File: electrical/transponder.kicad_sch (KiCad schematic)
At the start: 3 parts

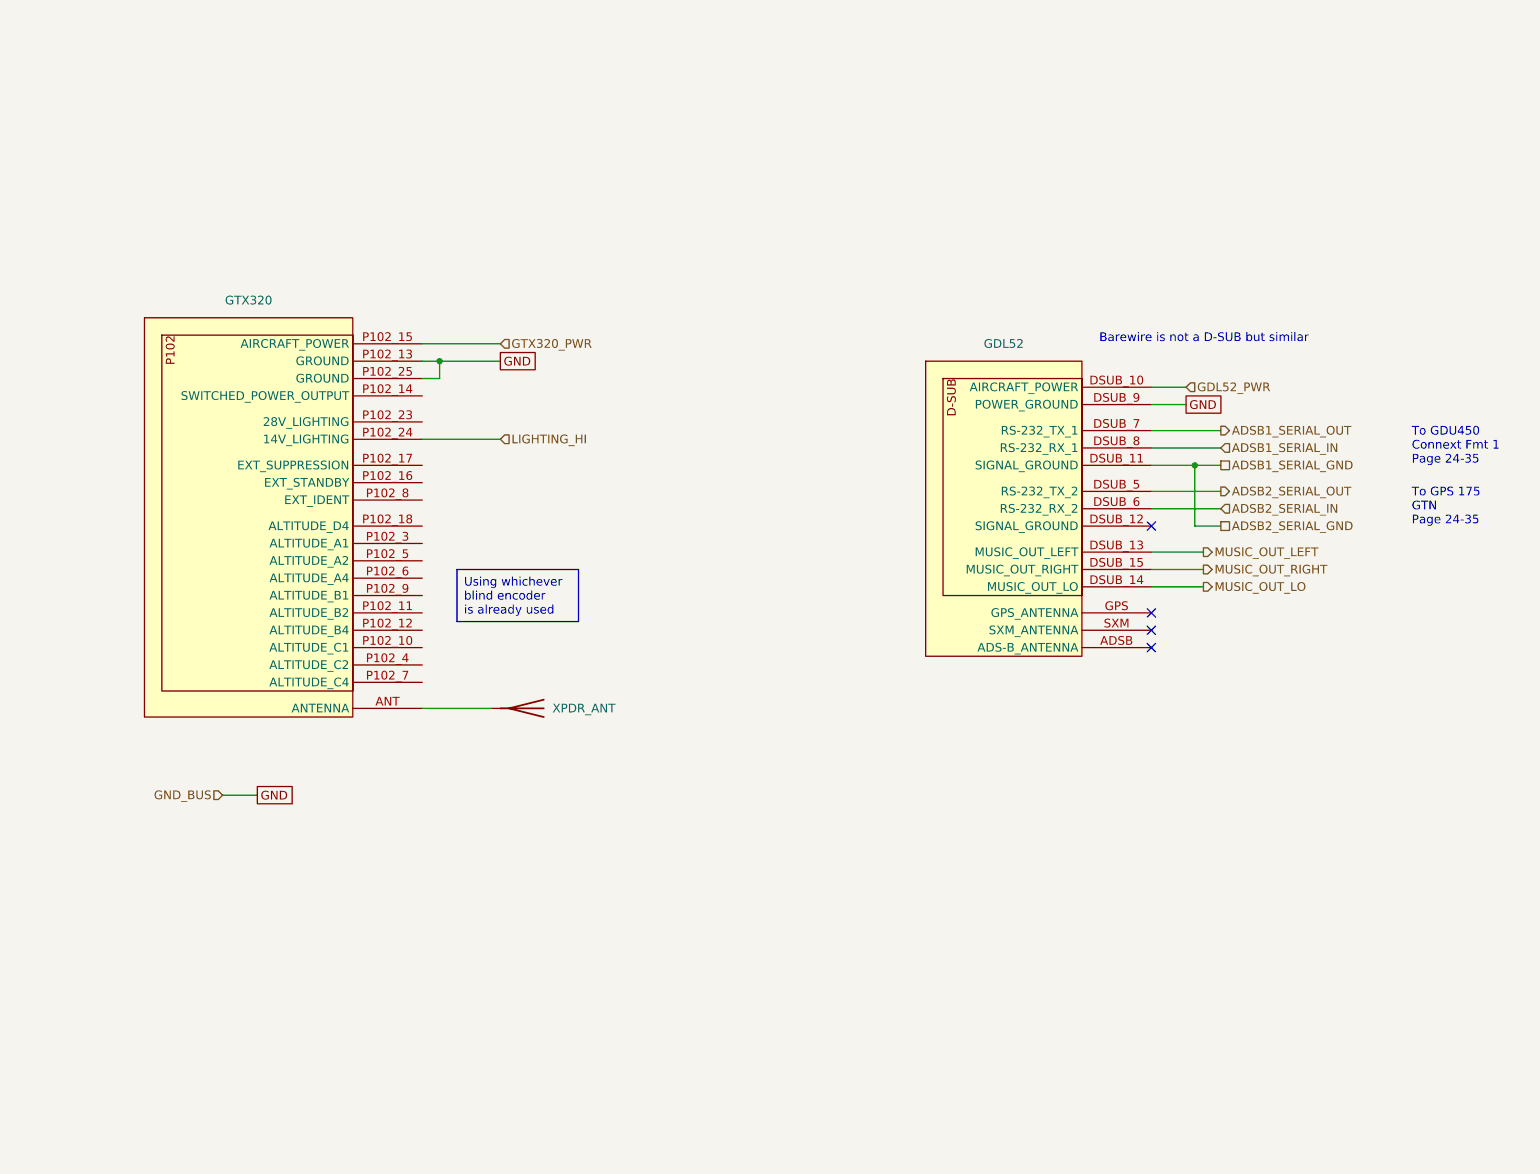
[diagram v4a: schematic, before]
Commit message: Added Altitude Encoder for 320, also added RS232 air data to Transponder in case upgrade to a GTX 327
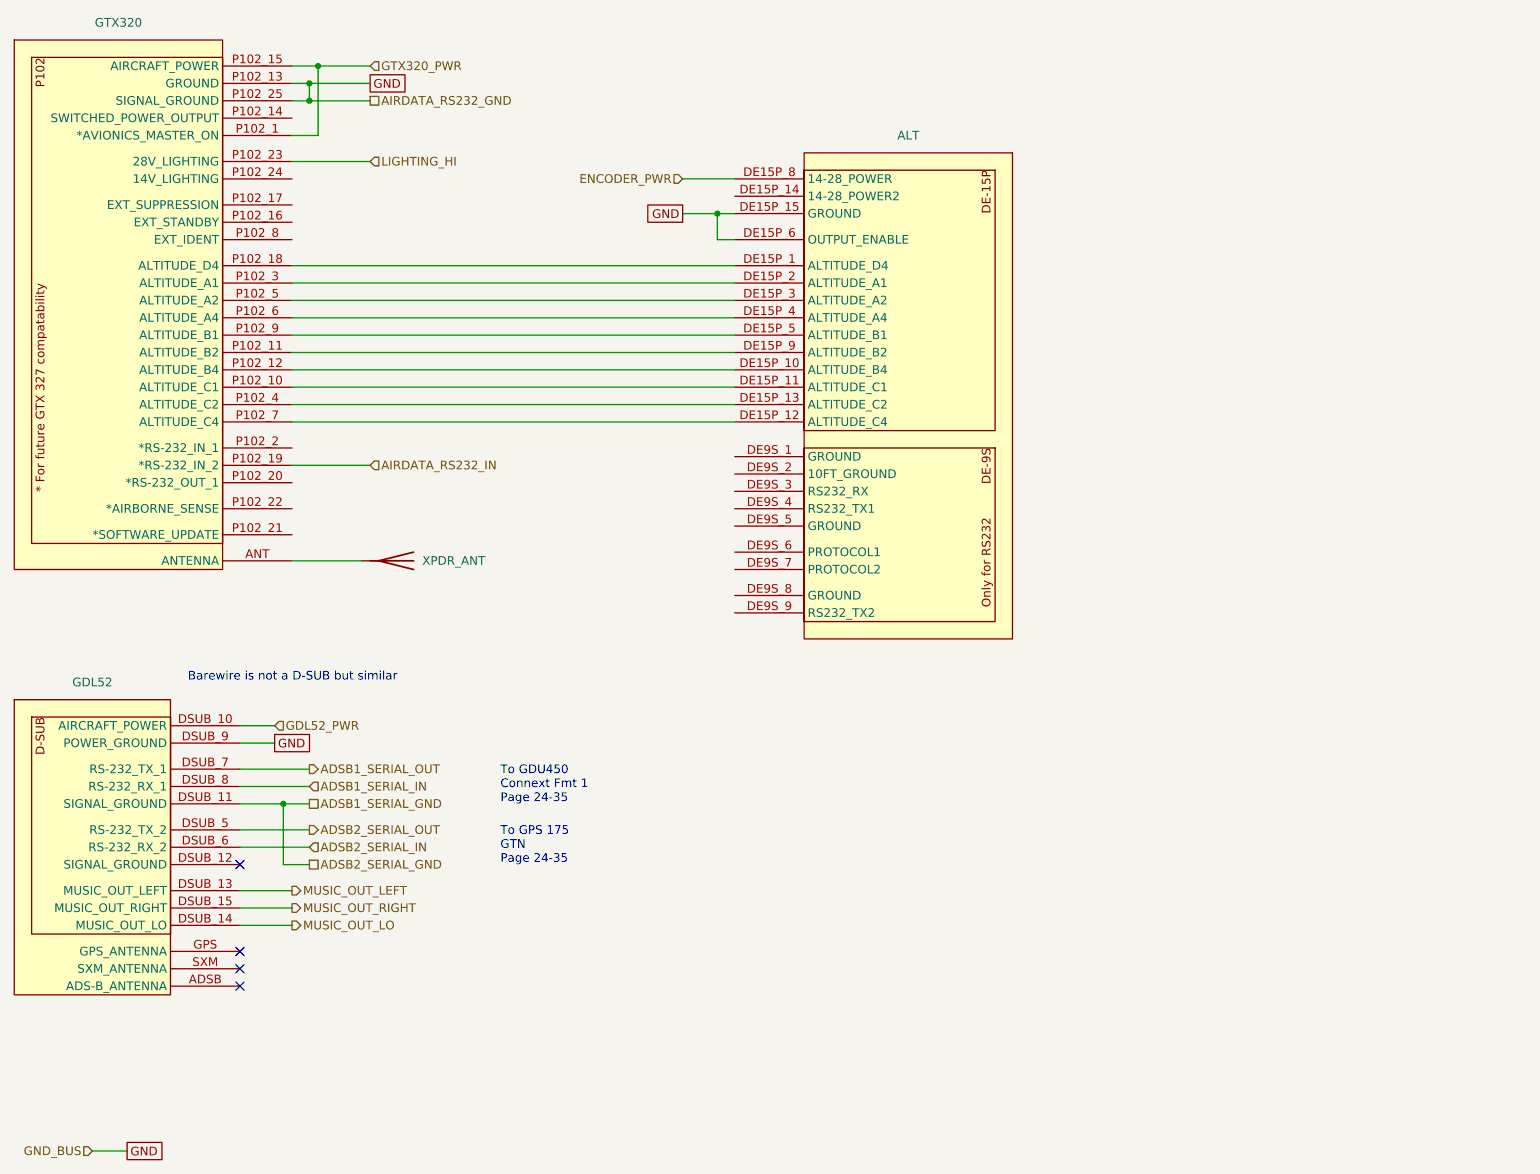
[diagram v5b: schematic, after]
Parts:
- added ALT: ~, symbol flyerx:TransCal_SSD120-30N
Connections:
- net GND: now also ALT.DE15P_15 (GROUND), ALT.DE15P_6 (OUTPUT_ENABLE)
- net GTX320_PWR: now also GTX320.P102_1 (*AVIONICS_MASTER_ON)
- net LIGHTING_HI: now also GTX320.P102_23 (28V_LIGHTING); no longer GTX320.P102_24 (14V_LIGHTING)
- net at GTX320.P102_10 (ALTITUDE_C1): now also ALT.DE15P_11 (ALTITUDE_C1)
- net at GTX320.P102_11 (ALTITUDE_B2): now also ALT.DE15P_9 (ALTITUDE_B2)
- net at GTX320.P102_12 (ALTITUDE_B4): now also ALT.DE15P_10 (ALTITUDE_B4)
- net at GTX320.P102_18 (ALTITUDE_D4): now also ALT.DE15P_1 (ALTITUDE_D4)
- net at GTX320.P102_3 (ALTITUDE_A1): now also ALT.DE15P_2 (ALTITUDE_A1)
- net at GTX320.P102_4 (ALTITUDE_C2): now also ALT.DE15P_13 (ALTITUDE_C2)
- net at GTX320.P102_5 (ALTITUDE_A2): now also ALT.DE15P_3 (ALTITUDE_A2)
- net at GTX320.P102_6 (ALTITUDE_A4): now also ALT.DE15P_4 (ALTITUDE_A4)
- net at GTX320.P102_7 (ALTITUDE_C4): now also ALT.DE15P_12 (ALTITUDE_C4)
- net at GTX320.P102_9 (ALTITUDE_B1): now also ALT.DE15P_5 (ALTITUDE_B1)
- new net AIRDATA_RS232_IN: GTX320.P102_19 (*RS-232_IN_2)
- new net ENCODER_PWR: ALT.DE15P_8 (14-28_POWER)
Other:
- moved on the sheet: GDL52, XPDR_ANT
